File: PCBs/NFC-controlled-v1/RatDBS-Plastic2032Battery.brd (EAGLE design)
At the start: 27.9 x 19.1 mm, 21 parts

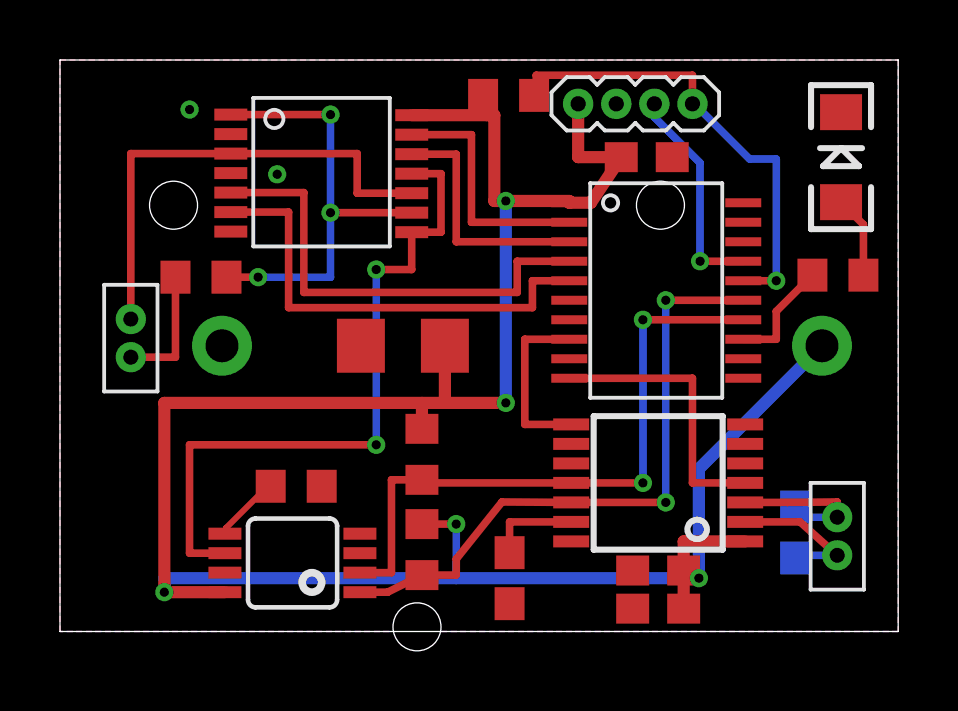
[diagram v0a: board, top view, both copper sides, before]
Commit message: Fixed board errors that were fixed in panelized version
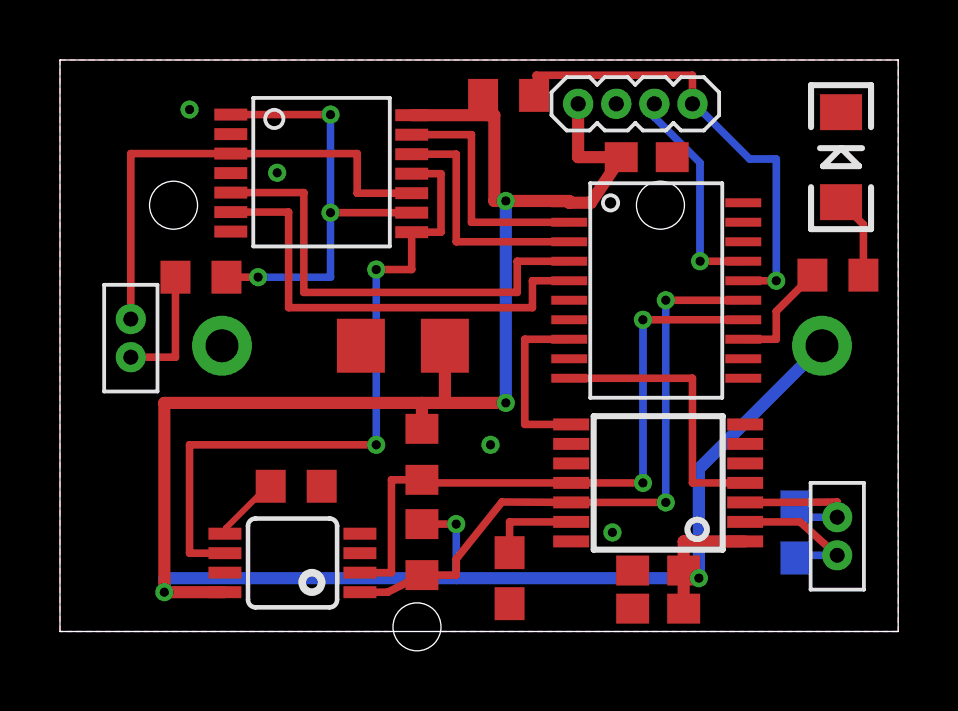
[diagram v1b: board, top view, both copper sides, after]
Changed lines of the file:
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@@
 </class>
 </classes>
-<designrules name="Seeed_DRU">
+<designrules name="Seeed_DRU *">
 <description language="de">&lt;b&gt;EAGLE Design Rules&lt;/b&gt;
 &lt;p&gt;
@@
 <param name="mtCopper" value="0.035mm 0.0175mm 0.035mm 0.035mm 0.035mm 0.035mm 0.035mm 0.035mm 0.035mm 0.035mm 0.035mm 0.035mm 0.035mm 0.035mm 0.0175mm 0.035mm"/>
 <param name="mtIsolate" value="1.5mm 1.1mm 0.2mm 0.15mm 0.2mm 0.15mm 0.2mm 0.15mm 0.2mm 0.15mm 0.2mm 0.15mm 0.2mm 0.15mm 0.2mm"/>
-<param name="mdWireWire" value="6mil"/>
-<param name="mdWirePad" value="6mil"/>
-<param name="mdWireVia" value="6mil"/>
-<param name="mdPadPad" value="6mil"/>
-<param name="mdPadVia" value="6mil"/>
-<param name="mdViaVia" value="6mil"/>
+<param name="mdWireWire" value="8mil"/>
+<param name="mdWirePad" value="8mil"/>
+<param name="mdWireVia" value="8mil"/>
+<param name="mdPadPad" value="8mil"/>
+<param name="mdPadVia" value="8mil"/>
+<param name="mdViaVia" value="8mil"/>
 <param name="mdSmdPad" value="0mil"/>
 <param name="mdSmdVia" value="0mil"/>
@@
 <wire x1="13.208" y1="1.778" x2="13.208" y2="3.5805" width="0.254" layer="16"/>
 <wire x1="13.208" y1="1.778" x2="3.478" y2="1.778" width="0.4064" layer="16"/>
-<wire x1="12.065" y1="6.7555" x2="12.065" y2="7.62" width="0.4064" layer="1"/>
-<wire x1="12.83" y1="7.62" x2="3.478" y2="7.62" width="0.4064" layer="1"/>
 <via x="3.478" y="1.311" extent="1-16" drill="0.3048" shape="octagon"/>
 <wire x1="5.497" y1="1.311" x2="3.478" y2="1.311" width="0.4064" layer="1"/>
@@
 <via x="13.208" y="3.5805" extent="1-16" drill="0.3048" shape="octagon"/>
 <wire x1="3.478" y1="7.62" x2="3.478" y2="1.311" width="0.4064" layer="1"/>
-<wire x1="12.83" y1="7.62" x2="14.859" y2="7.62" width="0.4064" layer="1"/>
 <wire x1="14.859" y1="7.62" x2="14.859" y2="14.351" width="0.4064" layer="16"/>
 <via x="14.859" y="7.62" extent="1-16" drill="0.3048" shape="octagon"/>
@@
 <wire x1="25.4" y1="9.525" x2="21.297" y2="5.422" width="0.4064" layer="16"/>
 <wire x1="21.297" y1="5.422" x2="21.297" y2="1.778" width="0.4064" layer="16"/>
-<wire x1="12.83" y1="7.62" x2="12.065" y2="7.62" width="0" layer="19" extent="1-1"/>
+<wire x1="12.83" y1="7.62" x2="14.859" y2="7.62" width="0.4064" layer="1"/>
+<wire x1="12.83" y1="7.62" x2="12.065" y2="7.62" width="0.4064" layer="1"/>
+<wire x1="12.065" y1="6.7555" x2="12.065" y2="7.62" width="0.4064" layer="1"/>
+<wire x1="12.065" y1="7.62" x2="3.478" y2="7.62" width="0.4064" layer="1"/>
 </signal>
 <signal name="GND">
@@
 <vertex x="0" y="0"/>
 </polygon>
-<via x="7.239" y="15.24" extent="1-16" drill="0.3048" shape="octagon"/>
+<via x="7.239" y="15.2908" extent="1-16" drill="0.3048" shape="octagon"/>
 <contactref element="C1" pad="2"/>
 <contactref element="C3" pad="2"/>
+<via x="14.351" y="6.223" extent="1-16" drill="0.3048" shape="octagon"/>
+<via x="18.415" y="3.302" extent="1-16" drill="0.3048" shape="octagon"/>
 </signal>
 <signal name="TEST">
